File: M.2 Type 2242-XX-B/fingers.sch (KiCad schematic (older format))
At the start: 7 parts, among them U301 M.2_NGFF_Socket2_KeyB_SSIC_Ad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

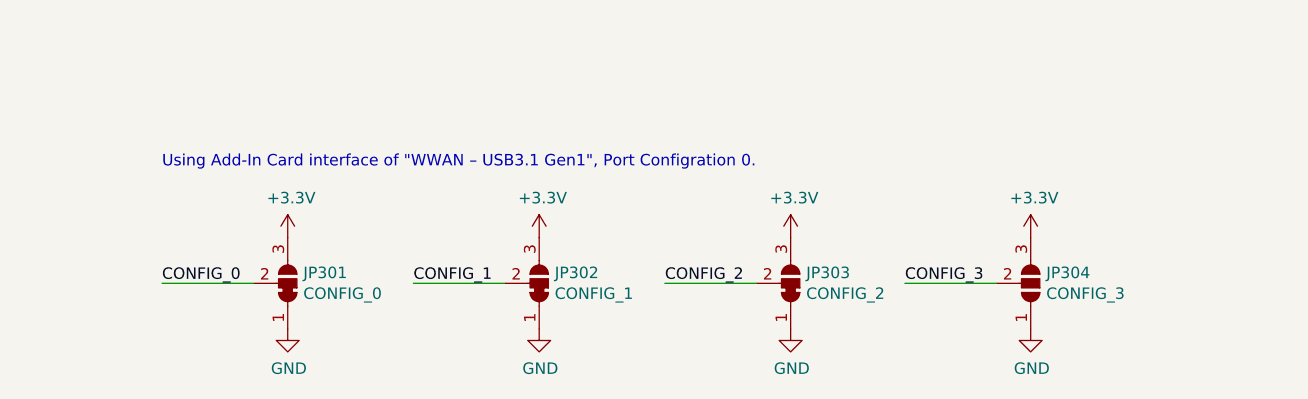
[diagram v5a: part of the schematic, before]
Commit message: Remove the solder pads for the config pins
Lets hope it is working as is. The board does not really have a lot of
real estate left...
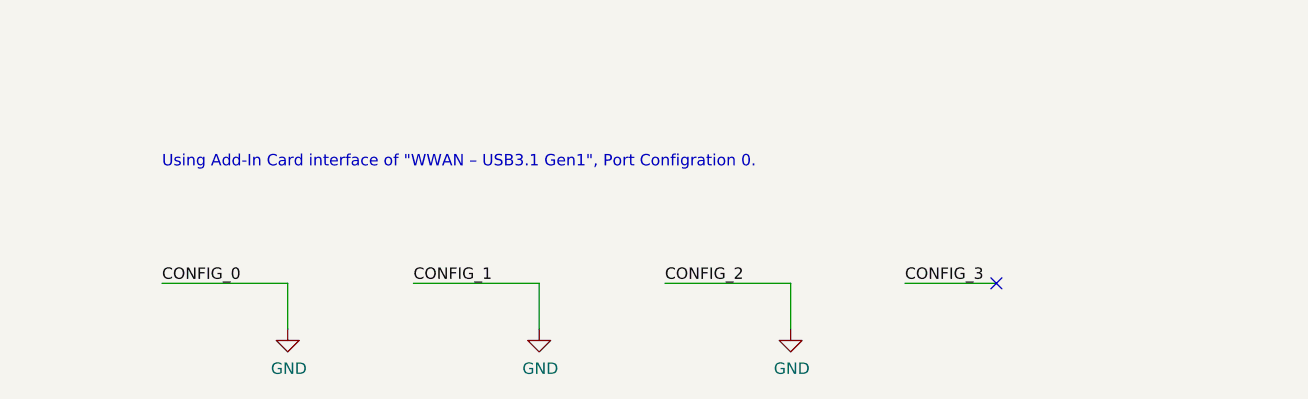
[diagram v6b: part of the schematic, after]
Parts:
- removed JP301: CONFIG_0, Jumper:SolderJumper-3_P1.3mm_Bridged12_RoundedPad1.0x1.5mm, symbol Jumper:SolderJumper_3_Bridged12
- removed JP302: CONFIG_1, Jumper:SolderJumper-3_P1.3mm_Bridged12_RoundedPad1.0x1.5mm, symbol Jumper:SolderJumper_3_Bridged12
- removed JP303: CONFIG_2, Jumper:SolderJumper-3_P1.3mm_Bridged12_RoundedPad1.0x1.5mm, symbol Jumper:SolderJumper_3_Bridged12
- removed JP304: CONFIG_3, Jumper:SolderJumper-3_P1.3mm_Open_RoundedPad1.0x1.5mm, symbol Jumper:SolderJumper_3_Open
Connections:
- net CONFIG_0 is gone; now on net GND: U301.21 (CONFIG_0)
- net CONFIG_1 is gone; now on net GND: U301.69 (CONFIG_1)
- net CONFIG_2 is gone; now on net GND: U301.75 (CONFIG_2)
- no-connect marks 26 -> 27
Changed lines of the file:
@@
-$EndComp
-$Comp
-L power:+3.3V #PWR0314
-U 1 1 5E0E23B3
-P 7250 5700
-F 0 "#PWR0314" H 7250 5550 50  0001 C CNN
-F 1 "+3.3V" H 7265 5873 50  0000 C CNN
-F 2 "" H 7250 5700 50  0001 C CNN
-F 3 "" H 7250 5700 50  0001 C CNN
-	1    7250 5700
-	1    0    0    -1
-$EndComp
-$Comp
-L Jumper:SolderJumper_3_Bridged12 JP301
-U 1 1 5E0DD0F3
-P 7250 5900
-F 0 "JP301" V 7296 5968 50  0000 L CNN
-F 1 "CONFIG_0" V 7205 5968 50  0000 L CNN
-F 2 "Jumper:SolderJumper-3_P1.3mm_Bridged12_RoundedPad1.0x1.5mm" H 7250 5900 50  0001 C CNN
-F 3 "~" H 7250 5900 50  0001 C CNN
-	1    7250 5900
-	0    1    -1   0
-$EndComp
-$Comp
-L Jumper:SolderJumper_3_Open JP304
-U 1 1 5E0E3B56
-P 10500 5900
-F 0 "JP304" V 10546 5968 50  0000 L CNN
-F 1 "CONFIG_3" V 10455 5968 50  0000 L CNN
-F 2 "Jumper:SolderJumper-3_P1.3mm_Open_RoundedPad1.0x1.5mm" H 10500 5900 50  0001 C CNN
-F 3 "~" H 10500 5900 50  0001 C CNN
-	1    10500 5900
-	0    1    -1   0
 $EndComp
 $Comp
@@
 	1    0    0    -1
 $EndComp
-$Comp
-L power:+3.3V #PWR0316
-U 1 1 5E0E6DCA
-P 8350 5700
-F 0 "#PWR0316" H 8350 5550 50  0001 C CNN
-F 1 "+3.3V" H 8365 5873 50  0000 C CNN
-F 2 "" H 8350 5700 50  0001 C CNN
-F 3 "" H 8350 5700 50  0001 C CNN
-	1    8350 5700
-	1    0    0    -1
-$EndComp
-$Comp
-L Jumper:SolderJumper_3_Bridged12 JP302
-U 1 1 5E0E6DD4
-P 8350 5900
-F 0 "JP302" V 8396 5968 50  0000 L CNN
-F 1 "CONFIG_1" V 8305 5968 50  0000 L CNN
-F 2 "Jumper:SolderJumper-3_P1.3mm_Bridged12_RoundedPad1.0x1.5mm" H 8350 5900 50  0001 C CNN
-F 3 "~" H 8350 5900 50  0001 C CNN
-	1    8350 5900
-	0    1    -1   0
-$EndComp
 Text Label 4950 4700 2    50   ~ 0
 CONFIG_0
@@
 Text Label 6700 5900 0    50   ~ 0
 CONFIG_0
-Wire Wire Line
-	6700 5900 7100 5900
 Text Label 7800 5900 0    50   ~ 0
 CONFIG_1
-Wire Wire Line
-	7800 5900 8200 5900
 $Comp
 L power:GND #PWR0319
@@
 	1    0    0    -1
 $EndComp
-$Comp
-L power:+3.3V #PWR0318
-U 1 1 5E0EB4C8
-P 9450 5700
-F 0 "#PWR0318" H 9450 5550 50  0001 C CNN
-F 1 "+3.3V" H 9465 5873 50  0000 C CNN
-F 2 "" H 9450 5700 50  0001 C CNN
-F 3 "" H 9450 5700 50  0001 C CNN
-	1    9450 5700
-	1    0    0    -1
-$EndComp
-$Comp
-L Jumper:SolderJumper_3_Bridged12 JP303
-U 1 1 5E0EB4D2
-P 9450 5900
-F 0 "JP303" V 9496 5968 50  0000 L CNN
-F 1 "CONFIG_2" V 9405 5968 50  0000 L CNN
-F 2 "Jumper:SolderJumper-3_P1.3mm_Bridged12_RoundedPad1.0x1.5mm" H 9450 5900 50  0001 C CNN
-F 3 "~" H 9450 5900 50  0001 C CNN
-	1    9450 5900
-	0    1    -1   0
-$EndComp
 Text Label 8900 5900 0    50   ~ 0
 CONFIG_2
-Wire Wire Line
-	8900 5900 9300 5900
 Text Label 9950 5900 0    50   ~ 0
 CONFIG_3
@@
 Wire Wire Line
 	4550 2300 4950 2300
-$Comp
-L power:GND #PWR0321
-U 1 1 5E0FBF8A
-P 10500 6100
-F 0 "#PWR0321" H 10500 5850 50  0001 C CNN
-F 1 "GND" H 10505 5927 50  0000 C CNN
-F 2 "" H 10500 6100 50  0001 C CNN
-F 3 "" H 10500 6100 50  0001 C CNN
-	1    10500 6100
-	1    0    0    -1
-$EndComp
-$Comp
-L power:+3.3V #PWR0320
-U 1 1 5E0FCD03
-P 10500 5700
-F 0 "#PWR0320" H 10500 5550 50  0001 C CNN
-F 1 "+3.3V" H 10515 5873 50  0000 C CNN
-F 2 "" H 10500 5700 50  0001 C CNN
-F 3 "" H 10500 5700 50  0001 C CNN
-	1    10500 5700
-	1    0    0    -1
-$EndComp
 Text Notes 6700 5400 0    50   ~ 0
 Using Add-In Card interface of "WWAN – USB3.1 Gen1", Port Configration 0.
@@
 	4650 2400 4550 2400
 NoConn ~ -3150 5500
+Wire Wire Line
+	7250 5900 7250 6100
+Wire Wire Line
+	6700 5900 7250 5900
+Wire Wire Line
+	8350 5900 8350 6100
+Wire Wire Line
+	7800 5900 8350 5900
+Wire Wire Line
+	9450 5900 9450 6100
+Wire Wire Line
+	8900 5900 9450 5900
+NoConn ~ 10350 5900
 $EndSCHEMATC

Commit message: Board more or less completely routed
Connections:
- net GND: no longer U301.33 (GND), U301.39 (GND), U301.45 (GND), U301.51 (GND), U301.57 (GND)
- no-connect marks 27 -> 32
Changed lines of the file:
@@
-$Comp
-L power:GND #PWR?
-U 1 1 5DCE827F
-P 4800 4100
-AR Path="/5DCE827F" Ref="#PWR?"  Part="1"
-AR Path="/5DCE3204/5DCE827F" Ref="#PWR0309"  Part="1"
-F 0 "#PWR0309" H 4800 3850 50  0001 C CNN
-F 1 "GND" H 4805 3927 50  0000 C CNN
-F 2 "" H 4800 4100 50  0001 C CNN
-F 3 "" H 4800 4100 50  0001 C CNN
-	1    4800 4100
-	1    0    0    -1
-$EndComp
-Wire Wire Line
-	4800 4100 4550 4100
-$Comp
-L power:GND #PWR?
-U 1 1 5DCE8286
-P 4800 3800
-AR Path="/5DCE8286" Ref="#PWR?"  Part="1"
-AR Path="/5DCE3204/5DCE8286" Ref="#PWR0308"  Part="1"
-F 0 "#PWR0308" H 4800 3550 50  0001 C CNN
-F 1 "GND" H 4805 3627 50  0000 C CNN
-F 2 "" H 4800 3800 50  0001 C CNN
-F 3 "" H 4800 3800 50  0001 C CNN
-	1    4800 3800
-	1    0    0    -1
-$EndComp
-Wire Wire Line
-	4800 3800 4550 3800
-$Comp
-L power:GND #PWR?
-U 1 1 5DCE828D
-P 4800 3500
-AR Path="/5DCE828D" Ref="#PWR?"  Part="1"
-AR Path="/5DCE3204/5DCE828D" Ref="#PWR0307"  Part="1"
-F 0 "#PWR0307" H 4800 3250 50  0001 C CNN
-F 1 "GND" H 4805 3327 50  0000 C CNN
-F 2 "" H 4800 3500 50  0001 C CNN
-F 3 "" H 4800 3500 50  0001 C CNN
-	1    4800 3500
-	1    0    0    -1
-$EndComp
-Wire Wire Line
-	4800 3500 4550 3500
-$Comp
-L power:GND #PWR?
-U 1 1 5DCE8294
-P 4800 3200
-AR Path="/5DCE8294" Ref="#PWR?"  Part="1"
-AR Path="/5DCE3204/5DCE8294" Ref="#PWR0306"  Part="1"
-F 0 "#PWR0306" H 4800 2950 50  0001 C CNN
-F 1 "GND" H 4805 3027 50  0000 C CNN
-F 2 "" H 4800 3200 50  0001 C CNN
-F 3 "" H 4800 3200 50  0001 C CNN
-	1    4800 3200
-	1    0    0    -1
-$EndComp
-Wire Wire Line
-	4800 3200 4550 3200
-$Comp
-L power:GND #PWR?
-U 1 1 5DCE829B
-P 4800 2900
-AR Path="/5DCE829B" Ref="#PWR?"  Part="1"
-AR Path="/5DCE3204/5DCE829B" Ref="#PWR0305"  Part="1"
-F 0 "#PWR0305" H 4800 2650 50  0001 C CNN
-F 1 "GND" H 4805 2727 50  0000 C CNN
-F 2 "" H 4800 2900 50  0001 C CNN
-F 3 "" H 4800 2900 50  0001 C CNN
-	1    4800 2900
-	1    0    0    -1
-$EndComp
-Wire Wire Line
-	4800 2900 4550 2900
 $Comp
 L power:GND #PWR?
@@
 	8900 5900 9450 5900
 NoConn ~ 10350 5900
+NoConn ~ 4550 4100
+NoConn ~ 4550 3800
+NoConn ~ 4550 3200
+NoConn ~ 4550 3500
+NoConn ~ 4550 2900
 $EndSCHEMATC
